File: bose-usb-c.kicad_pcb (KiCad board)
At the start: 4 copper layers, 24 x 16 mm, 37 parts, among them J1 502426-2030, J2 TYPE-C-31-M-12, J3 51281-0594, Q1 BC846BM3T5G, U1 TPS25200

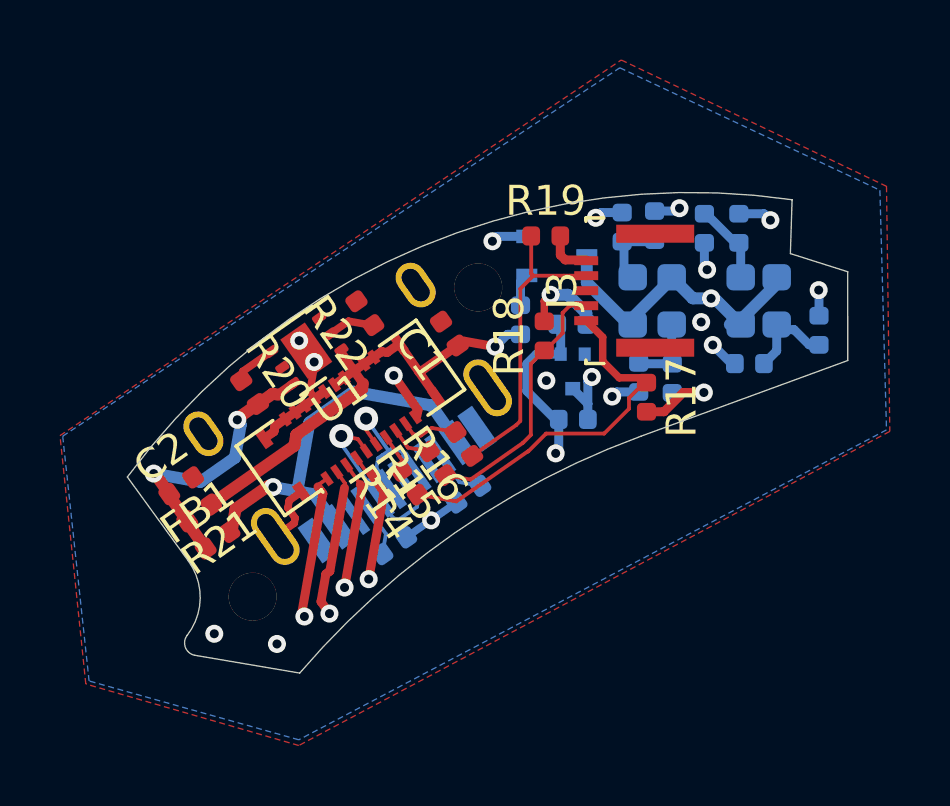
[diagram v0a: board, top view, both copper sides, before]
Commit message: Update files for KiCad V6
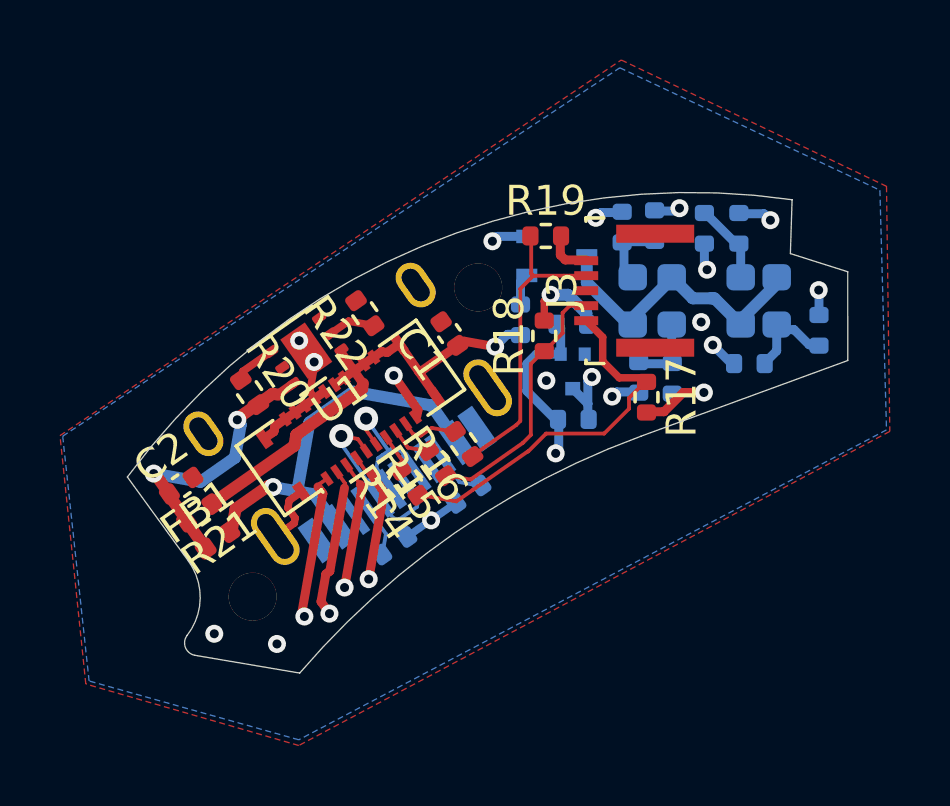
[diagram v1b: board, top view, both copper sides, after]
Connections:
- J2 pad A8: Net-(J2-PadA8) -> unconnected-(J2-PadA8)
- J2 pad B8: Net-(J2-PadB8) -> unconnected-(J2-PadB8)
- U1 pad 3: Net-(U1-Pad3) -> unconnected-(U1-Pad3)
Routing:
- net /LED_PWR: track 10.5 -> 10.1 mm, vias 1 -> 0
